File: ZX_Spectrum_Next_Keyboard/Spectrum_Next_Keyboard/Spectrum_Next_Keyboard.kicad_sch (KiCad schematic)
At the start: 62 parts, among them J1 TOP, J2 BOT, J3 2PIN

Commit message: Initial design completed
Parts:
- added H1, H2, H3, H4, H5, H6: MountingHole, MountingHole:MountingHole_3.2mm_M3, symbol Mechanical:MountingHole
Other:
- company: (none) -> Brett Hallen
- title: (none) -> ZX Spectrum Next Keyboard for Bare Board
- moved on the sheet: J1, J2, J3, KA1, KA10, KA11, KA12, KA13, KA2, KA3, KA4, KA5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

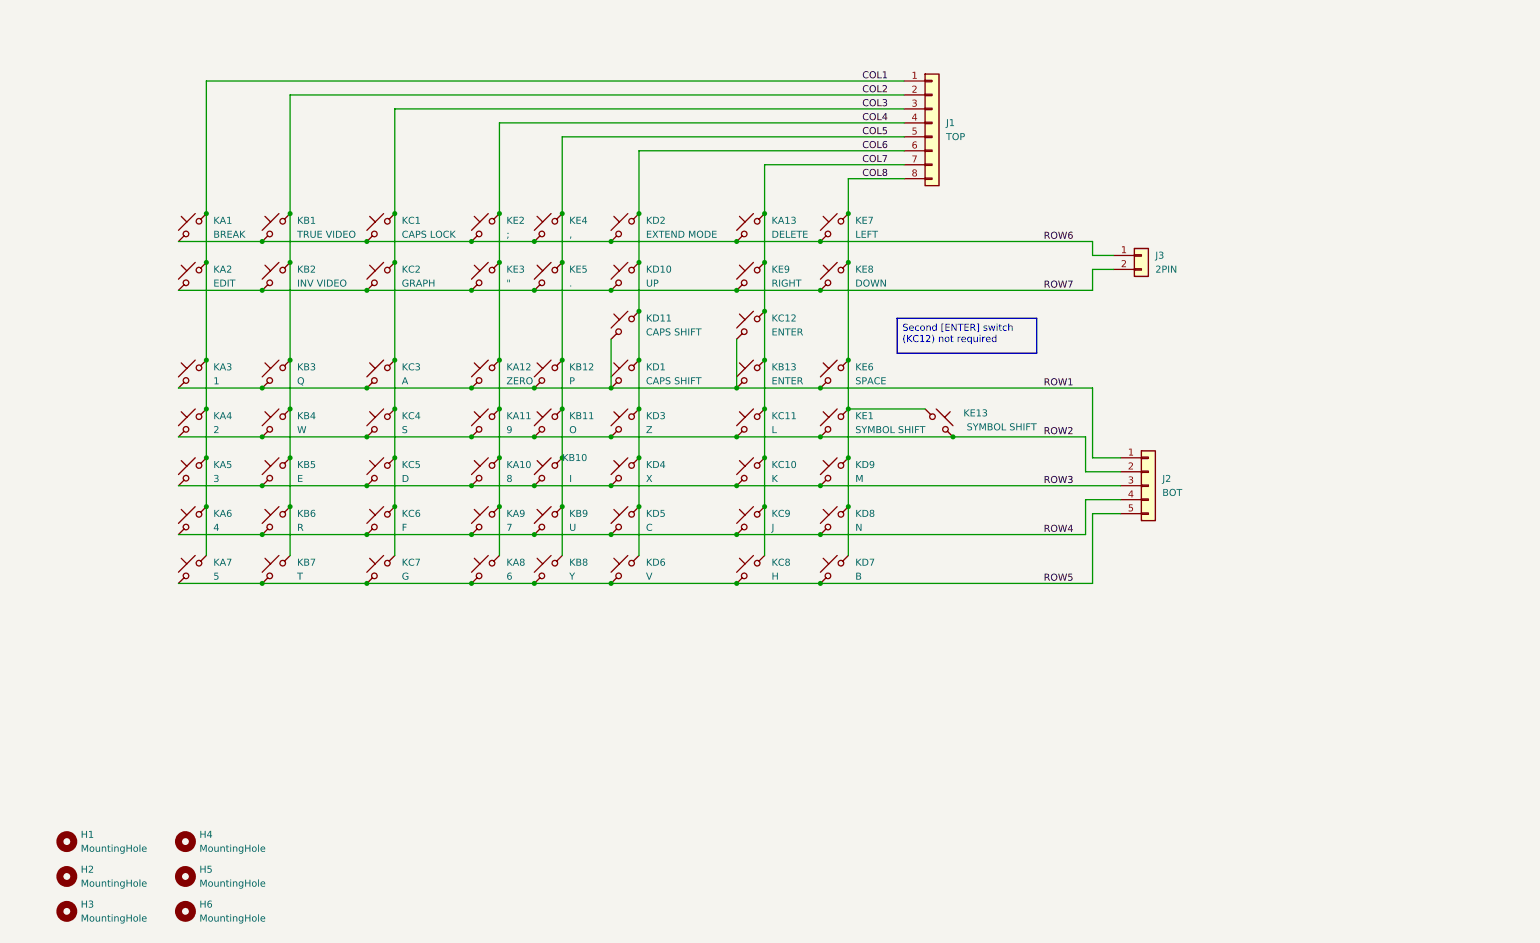
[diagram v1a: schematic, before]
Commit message: Added NumPad to keyboard
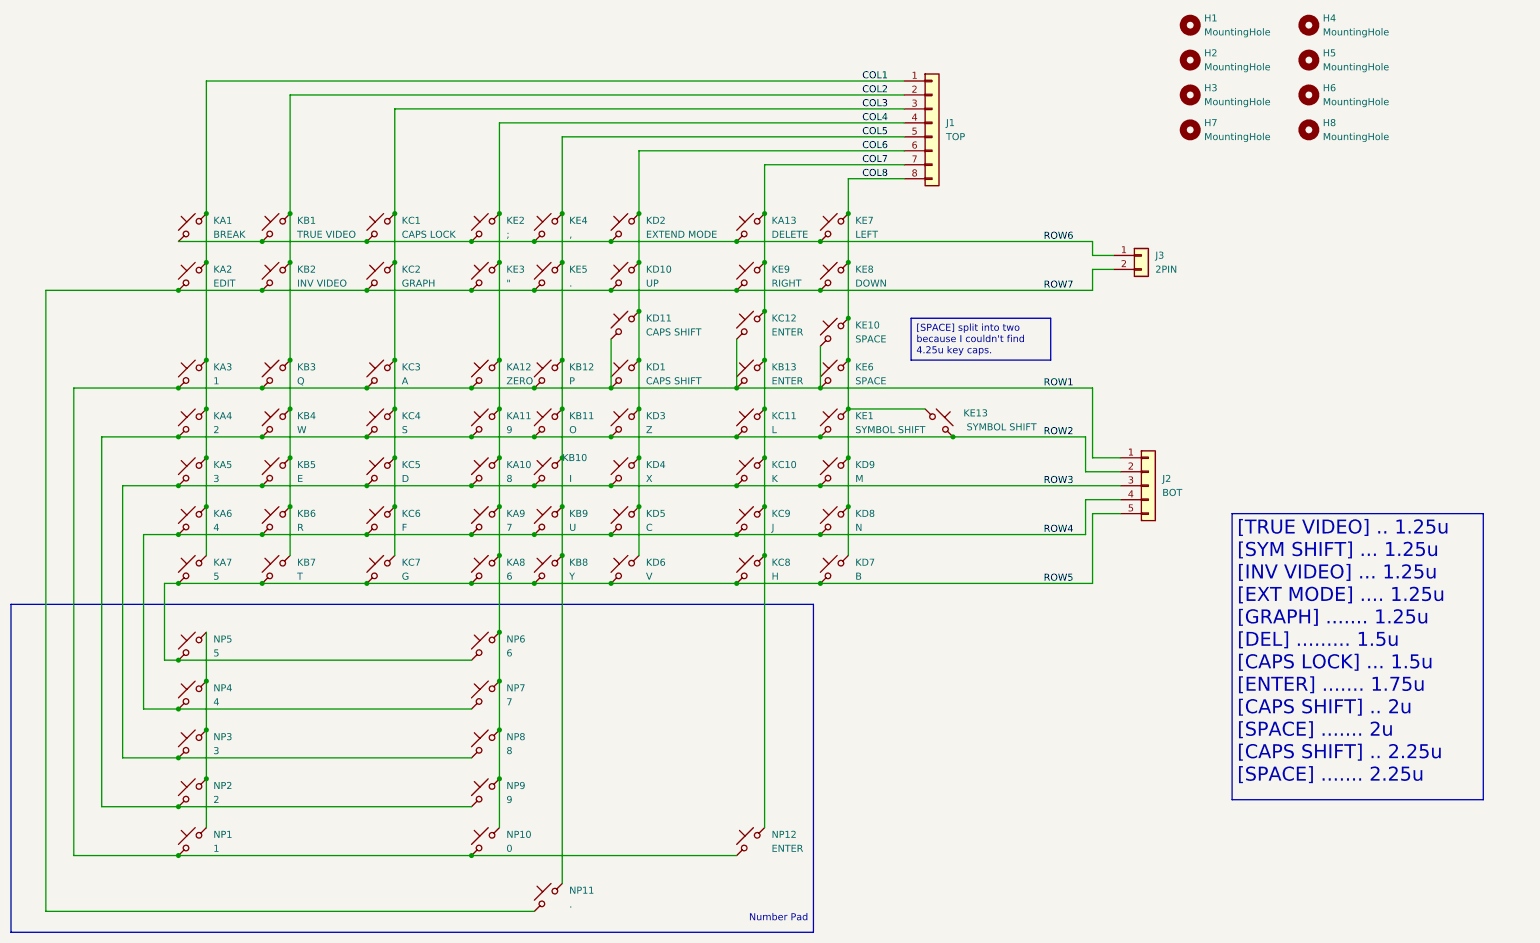
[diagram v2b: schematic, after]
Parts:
- added H7, H8: MountingHole, MountingHole:MountingHole_3.2mm_M3, symbol Mechanical:MountingHole
- added KE10: SPACE, Clueless_Engineer:SW_Gateron_LowProfile_THT, symbol Switch:SW_Push_45deg
- added NP1: 1, Clueless_Engineer:SW_Gateron_LowProfile_THT, symbol Switch:SW_Push_45deg
- added NP10: 0, Clueless_Engineer:SW_Gateron_LowProfile_THT, symbol Switch:SW_Push_45deg
- added NP11: ., Clueless_Engineer:SW_Gateron_LowProfile_THT, symbol Switch:SW_Push_45deg
- added NP12: ENTER, Clueless_Engineer:SW_Gateron_LowProfile_THT, symbol Switch:SW_Push_45deg
- added NP2: 2, Clueless_Engineer:SW_Gateron_LowProfile_THT, symbol Switch:SW_Push_45deg
- added NP3: 3, Clueless_Engineer:SW_Gateron_LowProfile_THT, symbol Switch:SW_Push_45deg
- added NP4: 4, Clueless_Engineer:SW_Gateron_LowProfile_THT, symbol Switch:SW_Push_45deg
- added NP5: 5, Clueless_Engineer:SW_Gateron_LowProfile_THT, symbol Switch:SW_Push_45deg
- added NP6: 6, Clueless_Engineer:SW_Gateron_LowProfile_THT, symbol Switch:SW_Push_45deg
- added NP7: 7, Clueless_Engineer:SW_Gateron_LowProfile_THT, symbol Switch:SW_Push_45deg
- added NP8: 8, Clueless_Engineer:SW_Gateron_LowProfile_THT, symbol Switch:SW_Push_45deg
- added NP9: 9, Clueless_Engineer:SW_Gateron_LowProfile_THT, symbol Switch:SW_Push_45deg
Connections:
- net COL4: now also NP10.2, NP6.2, NP7.2, NP8.2, NP9.2
- net COL5: now also NP11.2
- net COL7: now also NP12.2
- net COL8: now also KE10.2
- net ROW1: now also KE10.1, NP1.1, NP10.1, NP12.1
- net ROW2: now also NP2.1, NP9.1
- net ROW3: now also NP3.1, NP8.1
- net ROW4: now also NP4.1, NP7.1
- net ROW5: now also NP5.1, NP6.1
- net ROW7: now also NP11.1
- new net: NP1.2, NP2.2, NP3.2, NP4.2, NP5.2
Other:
- moved on the sheet: H1, H2, H3, H4, H5, H6
